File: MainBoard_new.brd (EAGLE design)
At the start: 59 parts, among them U1 STM32F10XRXT6, Y1 8MHz, Y2 32.768kHz

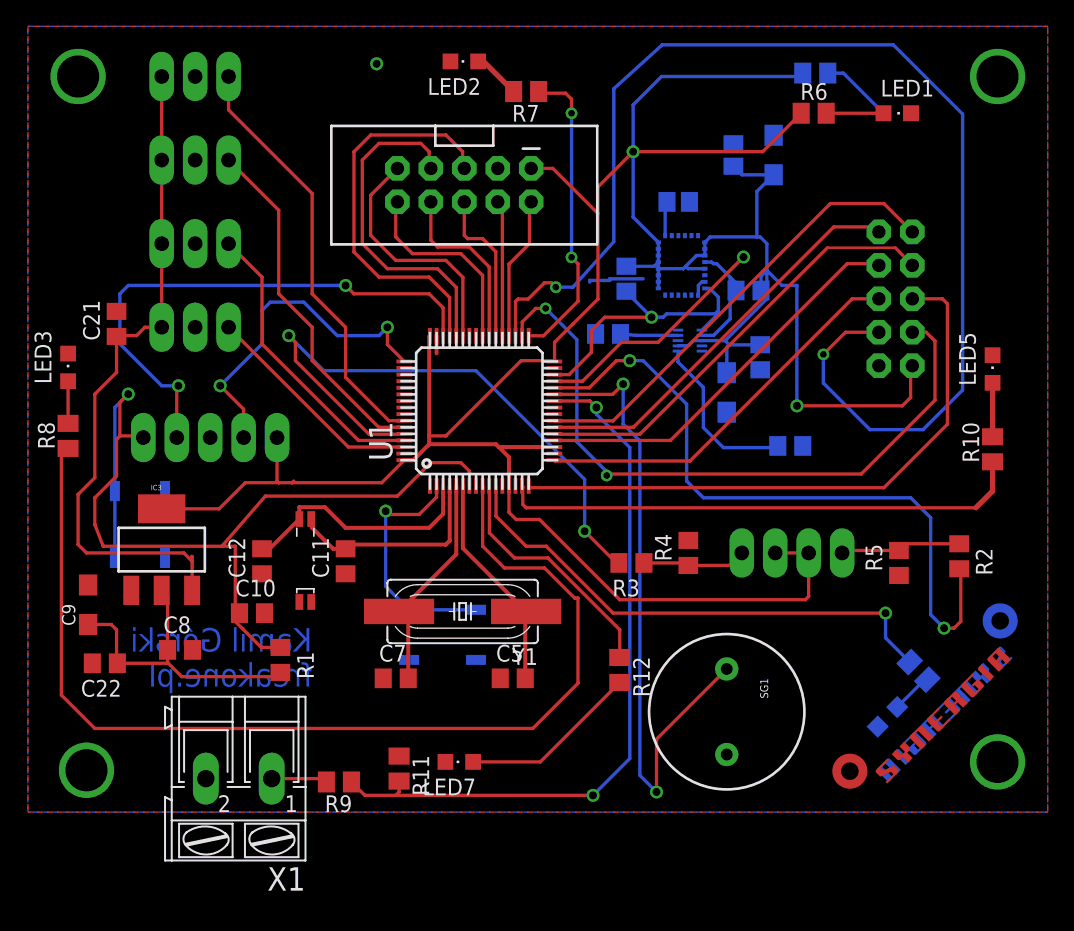
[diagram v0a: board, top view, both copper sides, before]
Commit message: kompresja płytki, dodany npn do buzzera
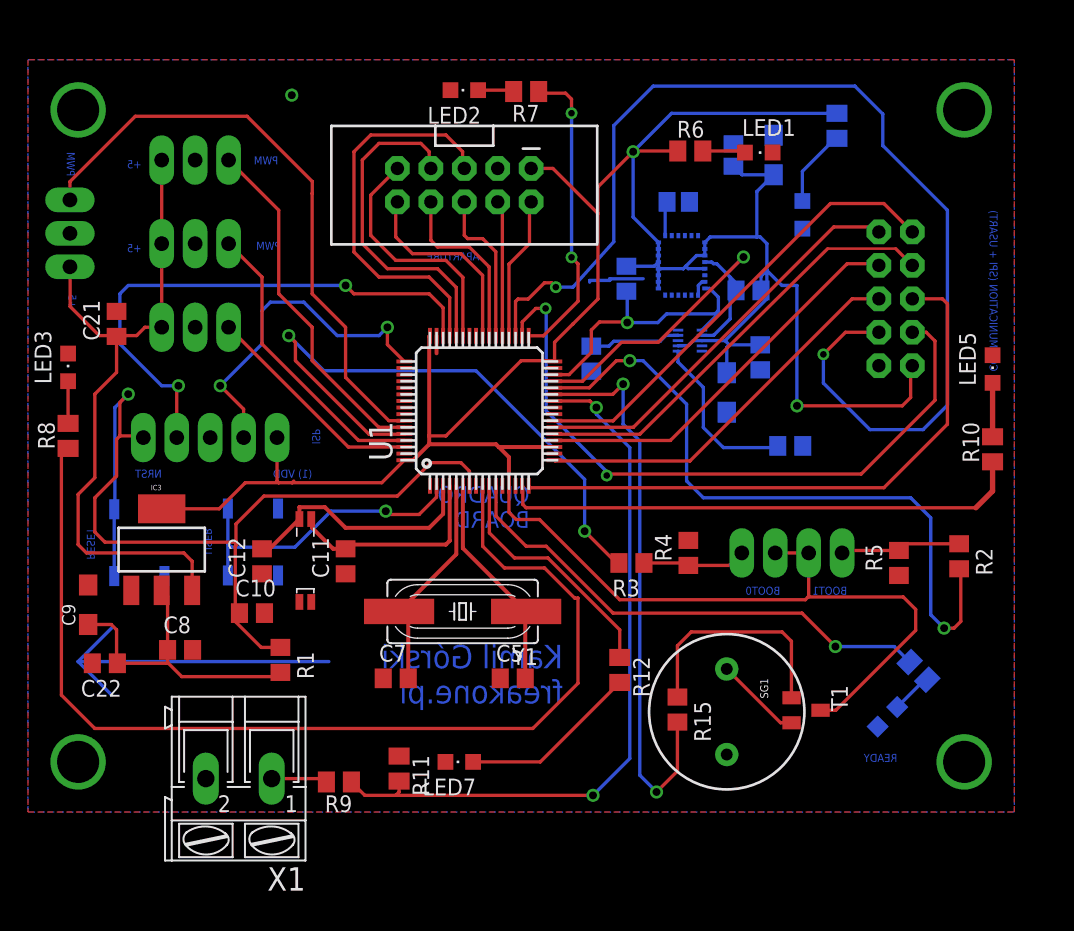
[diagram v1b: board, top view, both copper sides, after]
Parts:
- removed U$1, U$2: (no value), synergia_logo:SYNERGIA_16MM
- added R15: (no value), rcl:R0805
- added T1: BC847, transistor:SOT23
- moved JP5 16.1 mm to (-6.97, 44.0), turned to 90 degrees
- moved S3 16.0 mm to (6.93, 23.1), turned to 270 degrees
- moved LED1 10.9 mm to (45.4, 52.6)
- moved LED9 10.6 mm to (48.7, 47.9), turned to 180 degrees
- moved R6 9.80 mm to (40.2, 52.8)
- moved R14 4.33 mm to (51.3, 54.7), turned to 270 degrees
- moved C15 2.27 mm to (32.6, 37.0), turned to 90 degrees
- moved LED2 2.18 mm to (23.0, 57.4)
- moved S2 1.38 mm to (-1.70, 23.0)
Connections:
- new net N$17: SG1.-, T1.2
- new net N$20: R15.1, T1.1
- net 3.3V: now also T1.3
- net BUZZ: now also R15.2; no longer SG1.-
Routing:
- net N$18: track 0.00 -> 26.2 mm
- net N$20: track 0.00 -> 17.6 mm
- net REG1: track 32.4 -> 45.7 mm
- net OUT1: track 95.3 -> 86.6 mm
- net 3.3V: track 249.2 -> 257.8 mm
- net N$17: track 0.00 -> 6.62 mm
- net BUZZ: track 49.1 -> 43.6 mm
- net BUTTON: track 18.7 -> 23.7 mm
- net N$3: track 4.37 -> 6.92 mm
- net L7: track 39.4 -> 38.3 mm
- net N$6: track 4.35 -> 3.25 mm
- net NRST: track 70.8 -> 71.8 mm
- net N$7: track 3.65 -> 2.74 mm
- net 5V: track 51.6 -> 52.4 mm
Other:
- board text added: "(1) VDD"
- board text added: "+5"
- board text added: "APARTURE"
- board text added: "BOOT0"
- board text added: "BOOT1"
- board text added: "COMMUNICATION (SPI + USART)"
- board text added: "ISP"
- board text added: "NRST"
- board text added: "PWM"
- board text added: "QUADRO BOARD"
- board text added: "READY"
- board text added: "RESET"
- board text added: "USER"
